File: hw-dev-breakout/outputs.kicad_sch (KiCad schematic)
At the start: 67 parts, among them J301 WAGO 250-220, J302 Conn_01x20, Q301 2N7002, Q302 2N7002, Q303 2N7002, Q304 2N7002, Q305 2N7002, Q306 2N7002, Q307 2N7002, Q308 HL 20N04, Q309 HL 20N04, Q310 2N7002, Q311 Q_PMOS_HL_4485

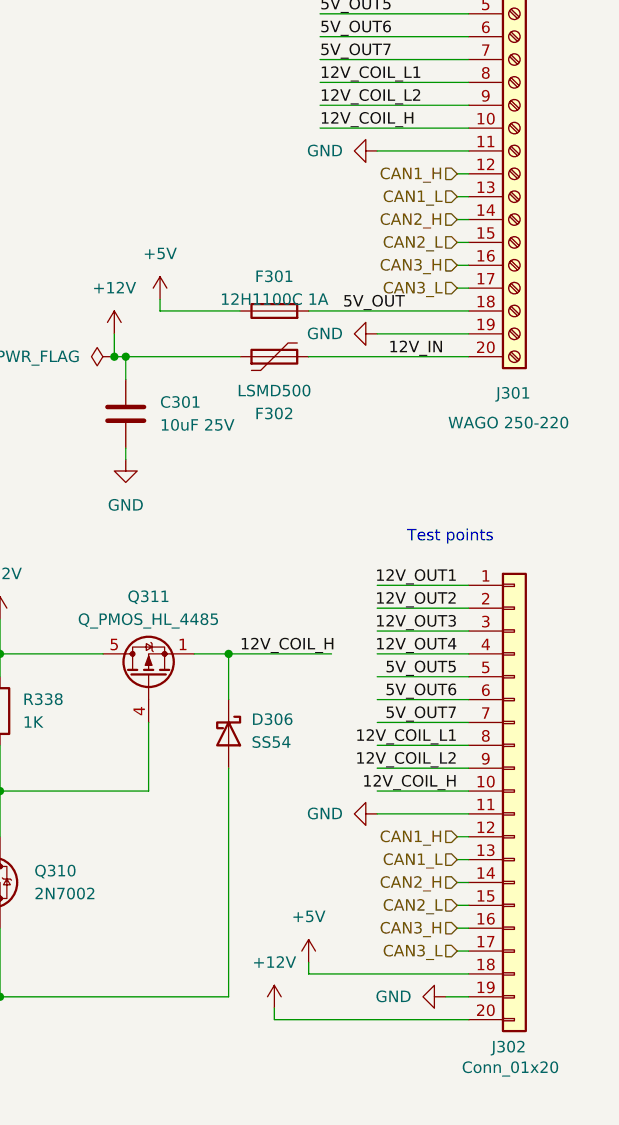
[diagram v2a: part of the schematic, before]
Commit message: pcb: Partially routed
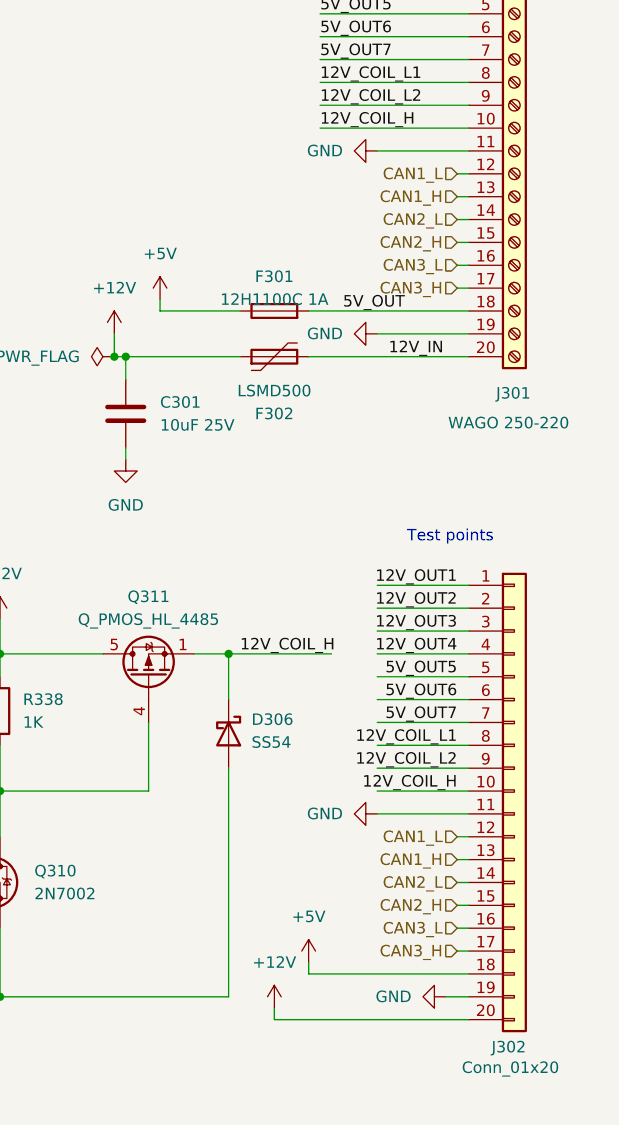
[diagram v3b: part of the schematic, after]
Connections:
- net CAN1_H: now also J301.13 (Pin_13), J302.13 (Pin_13); no longer J301.12 (Pin_12), J302.12 (Pin_12)
- net CAN1_L: now also J301.12 (Pin_12), J302.12 (Pin_12); no longer J301.13 (Pin_13), J302.13 (Pin_13)
- net CAN2_H: now also J301.15 (Pin_15), J302.15 (Pin_15); no longer J301.14 (Pin_14), J302.14 (Pin_14)
- net CAN2_L: now also J301.14 (Pin_14), J302.14 (Pin_14); no longer J301.15 (Pin_15), J302.15 (Pin_15)
- net CAN3_H: now also J301.17 (Pin_17), J302.17 (Pin_17); no longer J301.16 (Pin_16), J302.16 (Pin_16)
- net CAN3_L: now also J301.16 (Pin_16), J302.16 (Pin_16); no longer J301.17 (Pin_17), J302.17 (Pin_17)
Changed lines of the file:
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@@
 	(hierarchical_label "CAN3_H"
 		(shape input)
+		(at 269.24 143.51 180)
+		(fields_autoplaced yes)
+		(effects
+			(font
+				(size 1.27 1.27)
+			)
+			(justify right)
+		)
+	)
+	(hierarchical_label "OUT3"
+		(shape input)
+		(at 80.01 54.61 180)
+		(fields_autoplaced yes)
+		(effects
+			(font
+				(size 1.27 1.27)
+			)
+			(justify right)
+		)
+	)
+	(hierarchical_label "COIL_L2"
+		(shape input)
+		(at 148.59 62.23 180)
+		(fields_autoplaced yes)
+		(effects
+			(font
+				(size 1.27 1.27)
+			)
+			(justify right)
+		)
+	)
+	(hierarchical_label "CAN2_H"
+		(shape input)
+		(at 269.24 138.43 180)
+		(fields_autoplaced yes)
+		(effects
+			(font
+				(size 1.27 1.27)
+			)
+			(justify right)
+		)
+	)
+	(hierarchical_label "OUT1"
+		(shape input)
+		(at 21.59 53.34 180)
+		(fields_autoplaced yes)
+		(effects
+			(font
+				(size 1.27 1.27)
+			)
+			(justify right)
+		)
+	)
+	(hierarchical_label "CAN1_L"
+		(shape input)
+		(at 269.24 130.81 180)
+		(fields_autoplaced yes)
+		(effects
+			(font
+				(size 1.27 1.27)
+			)
+			(justify right)
+		)
+	)
+	(hierarchical_label "OUT7"
+		(shape input)
+		(at 130.81 165.1 180)
+		(fields_autoplaced yes)
+		(effects
+			(font
+				(size 1.27 1.27)
+			)
+			(justify right)
+		)
+	)
+	(hierarchical_label "CAN1_L"
+		(shape input)
+		(at 269.24 57.15 180)
+		(fields_autoplaced yes)
+		(effects
+			(font
+				(size 1.27 1.27)
+			)
+			(justify right)
+		)
+	)
+	(hierarchical_label "CAN2_H"
+		(shape input)
+		(at 269.24 64.77 180)
+		(fields_autoplaced yes)
+		(effects
+			(font
+				(size 1.27 1.27)
+			)
+			(justify right)
+		)
+	)
+	(hierarchical_label "CAN2_L"
+		(shape input)
+		(at 269.24 62.23 180)
+		(fields_autoplaced yes)
+		(effects
+			(font
+				(size 1.27 1.27)
+			)
+			(justify right)
+		)
+	)
+	(hierarchical_label "CAN3_H"
+		(shape input)
+		(at 269.24 69.85 180)
+		(fields_autoplaced yes)
+		(effects
+			(font
+				(size 1.27 1.27)
+			)
+			(justify right)
+		)
+	)
+	(hierarchical_label "CAN1_H"
+		(shape input)
+		(at 269.24 133.35 180)
+		(fields_autoplaced yes)
+		(effects
+			(font
+				(size 1.27 1.27)
+			)
+			(justify right)
+		)
+	)
+	(hierarchical_label "CAN3_L"
+		(shape input)
+		(at 269.24 67.31 180)
+		(fields_autoplaced yes)
+		(effects
+			(font
+				(size 1.27 1.27)
+			)
+			(justify right)
+		)
+	)
+	(hierarchical_label "COIL_H"
+		(shape input)
+		(at 187.96 135.89 180)
+		(fields_autoplaced yes)
+		(effects
+			(font
+				(size 1.27 1.27)
+			)
+			(justify right)
+		)
+	)
+	(hierarchical_label "CAN3_L"
+		(shape input)
 		(at 269.24 140.97 180)
 		(fields_autoplaced yes)
@@
 		)
 	)
-	(hierarchical_label "OUT3"
-		(shape input)
-		(at 80.01 54.61 180)
-		(fields_autoplaced yes)
-		(effects
-			(font
-				(size 1.27 1.27)
-			)
-			(justify right)
-		)
-	)
-	(hierarchical_label "COIL_L2"
-		(shape input)
-		(at 148.59 62.23 180)
-		(fields_autoplaced yes)
-		(effects
-			(font
-				(size 1.27 1.27)
-			)
-			(justify right)
-		)
-	)
-	(hierarchical_label "CAN2_H"
+	(hierarchical_label "OUT4"
+		(shape input)
+		(at 80.01 107.95 180)
+		(fields_autoplaced yes)
+		(effects
+			(font
+				(size 1.27 1.27)
+			)
+			(justify right)
+		)
+	)
+	(hierarchical_label "CAN2_L"
 		(shape input)
 		(at 269.24 135.89 180)
@@
 		)
 	)
-	(hierarchical_label "OUT1"
-		(shape input)
-		(at 21.59 53.34 180)
-		(fields_autoplaced yes)
-		(effects
-			(font
-				(size 1.27 1.27)
-			)
-			(justify right)
-		)
-	)
-	(hierarchical_label "CAN1_L"
-		(shape input)
-		(at 269.24 133.35 180)
-		(fields_autoplaced yes)
-		(effects
-			(font
-				(size 1.27 1.27)
-			)
-			(justify right)
-		)
-	)
-	(hierarchical_label "OUT7"
-		(shape input)
-		(at 130.81 165.1 180)
-		(fields_autoplaced yes)
-		(effects
-			(font
-				(size 1.27 1.27)
-			)
-			(justify right)
-		)
-	)
-	(hierarchical_label "CAN1_L"
+	(hierarchical_label "OUT2"
+		(shape input)
+		(at 21.59 106.68 180)
+		(fields_autoplaced yes)
+		(effects
+			(font
+				(size 1.27 1.27)
+			)
+			(justify right)
+		)
+	)
+	(hierarchical_label "CAN1_H"
 		(shape input)
 		(at 269.24 59.69 180)
 		(fields_autoplaced yes)
 		(effects
-			(font
-				(size 1.27 1.27)
-			)
-			(justify right)
-		)
-	)
-	(hierarchical_label "CAN2_H"
-		(shape input)
-		(at 269.24 62.23 180)
-		(fields_autoplaced yes)
-		(effects
-			(font
-				(size 1.27 1.27)
-			)
-			(justify right)
-		)
-	)
-	(hierarchical_label "CAN2_L"
-		(shape input)
-		(at 269.24 64.77 180)
-		(fields_autoplaced yes)
-		(effects
-			(font
-				(size 1.27 1.27)
-			)
-			(justify right)
-		)
-	)
-	(hierarchical_label "CAN3_H"
-		(shape input)
-		(at 269.24 67.31 180)
-		(fields_autoplaced yes)
-		(effects
-			(font
-				(size 1.27 1.27)
-			)
-			(justify right)
-		)
-	)
-	(hierarchical_label "CAN1_H"
-		(shape input)
-		(at 269.24 130.81 180)
-		(fields_autoplaced yes)
-		(effects
-			(font
-				(size 1.27 1.27)
-			)
-			(justify right)
-		)
-	)
-	(hierarchical_label "CAN3_L"
-		(shape input)
-		(at 269.24 69.85 180)
-		(fields_autoplaced yes)
-		(effects
-			(font
-				(size 1.27 1.27)
-			)
-			(justify right)
-		)
-	)
-	(hierarchical_label "COIL_H"
-		(shape input)
-		(at 187.96 135.89 180)
-		(fields_autoplaced yes)
-		(effects
-			(font
-				(size 1.27 1.27)
-			)
-			(justify right)
-		)
-	)
-	(hierarchical_label "CAN3_L"
-		(shape input)
-		(at 269.24 143.51 180)
-		(fields_autoplaced yes)
-		(effects
-			(font
-				(size 1.27 1.27)
-			)
-			(justify right)
-		)
-	)
-	(hierarchical_label "OUT4"
-		(shape input)
-		(at 80.01 107.95 180)
-		(fields_autoplaced yes)
-		(effects
-			(font
-				(size 1.27 1.27)
-			)
-			(justify right)
-		)
-	)
-	(hierarchical_label "CAN2_L"
-		(shape input)
-		(at 269.24 138.43 180)
-		(fields_autoplaced yes)
-		(effects
-			(font
-				(size 1.27 1.27)
-			)
-			(justify right)
-		)
-	)
-	(hierarchical_label "OUT2"
-		(shape input)
-		(at 21.59 106.68 180)
-		(fields_autoplaced yes)
-		(effects
-			(font
-				(size 1.27 1.27)
-			)
-			(justify right)
-		)
-	)
-	(hierarchical_label "CAN1_H"
-		(shape input)
-		(at 269.24 57.15 180)
-		(fields_autoplaced yes)
-		(effects

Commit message: pcb: Routed for 2 layer, fixed P-fet error
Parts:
- J301: footprint hw-dev-breakout:CONN-TH_250-220 -> hw-dev-breakout:WAGO 250-22
- J302: now not fitted
- Q308, Q309: footprint Package_TO_SOT_SMD:TO-252-3_TabPin2 -> Package_TO_SOT_SMD:TO-252-2
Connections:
- net +12V: now also Q311.1 (S), Q311.2 (S), Q311.3 (S); no longer Q311.5 (D), Q311.6 (D), Q311.7 (D), Q311.8 (D)
- net 12V_COIL_H: now also Q311.5 (D), Q311.6 (D), Q311.7 (D), Q311.8 (D); no longer Q311.1 (S), Q311.2 (S), Q311.3 (S)
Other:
- moved on the sheet: Q311
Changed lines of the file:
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@@
 			)
 		)
-		(property "Footprint" "Package_TO_SOT_SMD:TO-252-3_TabPin2"
+		(property "Footprint" "Package_TO_SOT_SMD:TO-252-2"
 			(at 184.15 30.48 0)
 			(effects
@@
 			)
 		)
-		(property "Footprint" "Package_TO_SOT_SMD:TO-252-3_TabPin2"
+		(property "Footprint" "Package_TO_SOT_SMD:TO-252-2"
 			(at 184.15 59.69 0)
 			(effects
@@
 		(in_bom yes)
 		(on_board yes)
-		(dnp no)
+		(dnp yes)
 		(property "Reference" "J302"
 			(at 273.05 154.178 0)
@@
 	(symbol
 		(lib_id "hw-dev-breakout:Q_PMOS_HL_4485")
-		(at 234.95 113.03 90)
+		(at 234.95 113.03 270)
+		(mirror x)
 		(unit 1)
 		(exclude_from_sim no)
@@
 		(on_board yes)
 		(dnp no)
-		(fields_autoplaced yes)
 		(property "Reference" "Q311"
 			(at 234.95 104.14 90)
@@
 		)
 		(property "Footprint" "Package_SO:SOP-8_3.9x4.9mm_P1.27mm"
-			(at 247.904 109.982 0)
+			(at 221.996 109.982 0)
 			(effects
 				(font
@@
 		)
 		(property "Datasheet" "https://www.lcsc.com/datasheet/lcsc_datasheet_2310251707_HL-4485_C7499854.pdf"
-			(at 250.19 112.014 0)
+			(at 219.71 112.014 0)
 			(effects
 				(font
@@
 		)
 		(property "Description" "High cell density trenched P-ch MOSFET"
-			(at 248.666 111.76 0)
+			(at 221.234 111.76 0)
 			(effects
 				(font
@@
 			)
 		)
-		(property "Footprint" "hw-dev-breakout:CONN-TH_250-220"
+		(property "Footprint" "hw-dev-breakout:WAGO 250-22"
 			(at 275.59 52.07 0)
 			(effects

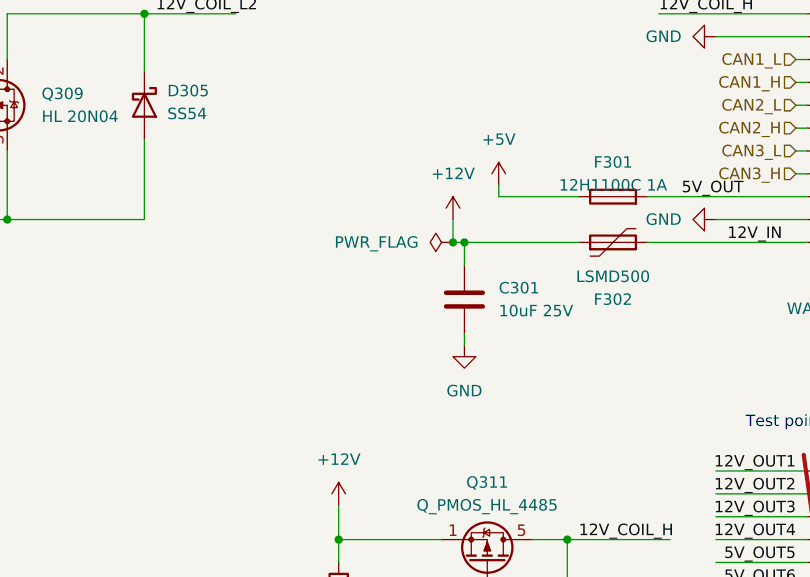
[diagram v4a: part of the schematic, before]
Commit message: Add reverse polarity protection for 12V In
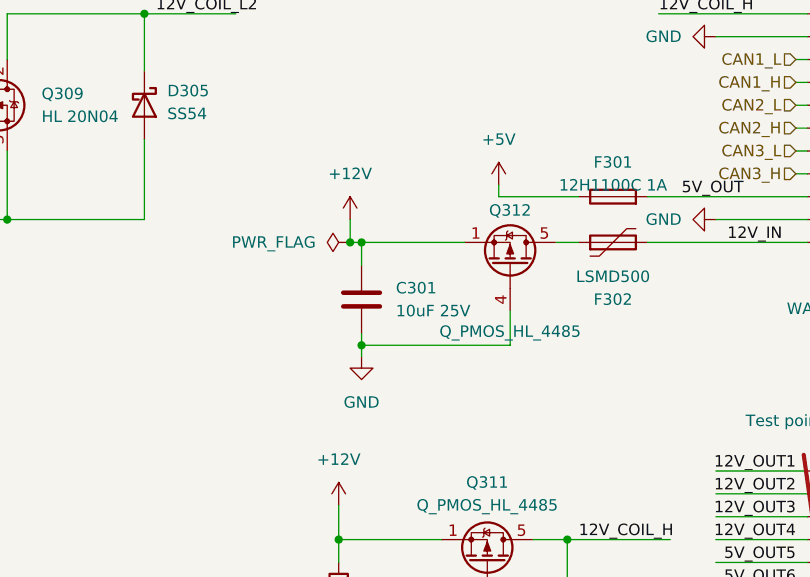
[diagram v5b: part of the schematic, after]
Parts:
- added Q312: Q_PMOS_HL_4485, Package_SO:SOP-8_3.9x4.9mm_P1.27mm, symbol hw-dev-breakout:Q_PMOS_HL_4485
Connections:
- net +12V: now also Q312.1 (S), Q312.2 (S), Q312.3 (S); no longer F302.1
- net GND: now also Q312.4 (G)
- new net: F302.1, Q312.5 (D), Q312.6 (D), Q312.7 (D), Q312.8 (D)
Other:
- moved on the sheet: C301
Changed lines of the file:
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@@
 	)
 	(junction
+		(at 220.98 88.9)
+		(diameter 0)
+		(color 0 0 0 0)
+	)
+	(junction
 		(at 196.85 22.86)
 		(diameter 0)
@@
 	)
 	(junction
+		(at 220.98 77.47)
+		(diameter 0)
+		(color 0 0 0 0)
+	)
+	(junction
 		(at 198.12 135.89)
 		(diameter 0)
@@
 	)
 	(junction
-		(at 231.14 77.47)
+		(at 219.71 77.47)
 		(diameter 0)
 		(color 0 0 0 0)
@@
 		(color 0 0 0 0)
 	)
-	(junction
-		(at 232.41 77.47)
-		(diameter 0)
-		(color 0 0 0 0)
-	)
 	(wire
 		(pts
@@
 	(wire
 		(pts
+			(xy 237.49 85.09) (xy 237.49 88.9)
+		)
+		(stroke
+			(width 0)
+			(type default)
+		)
+	)
+	(wire
+		(pts
 			(xy 48.26 24.13) (xy 48.26 25.4)
 		)
@@
 	(wire
 		(pts
+			(xy 220.98 88.9) (xy 220.98 90.17)
+		)
+		(stroke
+			(width 0)
+			(type default)
+		)
+	)
+	(wire
+		(pts
 			(xy 161.29 62.23) (xy 161.29 63.5)
 		)
@@
 	(wire
 		(pts
+			(xy 220.98 87.63) (xy 220.98 88.9)
+		)
+		(stroke
+			(width 0)
+			(type default)
+		)
+	)
+	(wire
+		(pts
 			(xy 161.29 71.12) (xy 161.29 74.93)
 		)
@@
 	(wire
 		(pts
-			(xy 232.41 77.47) (xy 245.11 77.47)
-		)
-		(stroke
-			(width 0)
-			(type default)
-		)
-	)
-	(wire
-		(pts
 			(xy 48.26 33.02) (xy 48.26 35.56)
 		)
@@
 	(wire
 		(pts
+			(xy 237.49 88.9) (xy 220.98 88.9)
+		)
+		(stroke
+			(width 0)
+			(type default)
+		)
+	)
+	(wire
+		(pts
 			(xy 161.29 33.02) (xy 161.29 34.29)
 		)
@@
 	(wire
 		(pts
-			(xy 232.41 77.47) (xy 232.41 80.01)
+			(xy 220.98 77.47) (xy 220.98 80.01)
 		)
 		(stroke
@@
 	(wire
 		(pts
-			(xy 231.14 77.47) (xy 232.41 77.47)
+			(xy 219.71 77.47) (xy 220.98 77.47)
 		)
 		(stroke
@@
 	(wire
 		(pts
-			(xy 231.14 74.93) (xy 231.14 77.47)
+			(xy 219.71 74.93) (xy 219.71 77.47)
 		)
 		(stroke
@@
 	(wire
 		(pts
-			(xy 232.41 87.63) (xy 232.41 88.9)
-		)
-		(stroke
-			(width 0)
-			(type default)
-		)
-	)
-	(wire
-		(pts
 			(xy 157.48 160.02) (xy 157.48 154.94)
 		)
@@
 	(wire
 		(pts
+			(xy 220.98 77.47) (xy 232.41 77.47)
+		)
+		(stroke
+			(width 0)
+			(type default)
+		)
+	)
+	(wire
+		(pts
+			(xy 242.57 77.47) (xy 245.11 77.47)
+		)
+		(stroke
+			(width 0)
+			(type default)
+		)
+	)
+	(wire
+		(pts
 			(xy 48.26 66.04) (xy 48.26 58.42)
 		)
@@
 	(symbol
 		(lib_id "Device:C")
-		(at 232.41 83.82 0)
+		(at 220.98 83.82 0)
 		(unit 1)
 		(exclude_from_sim no)
@@
 		(fields_autoplaced yes)
 		(property "Reference" "C301"
-			(at 236.22 82.5499 0)
+			(at 224.79 82.5499 0)
 			(effects
 				(font
@@
 		)
 		(property "Value" "10uF 25V"
-			(at 236.22 85.0899 0)
+			(at 224.79 85.0899 0)
 			(effects
 				(font
@@
 		)
 		(property "Footprint" "Capacitor_SMD:CP_Elec_4x4.5"
-			(at 233.3752 87.63 0)
+			(at 221.9452 87.63 0)
 			(effects
 				(font
@@
 		)
 		(property "Datasheet" "~"
-			(at 232.41 83.82 0)
+			(at 220.98 83.82 0)
 			(effects
 				(font
@@
 		)
 		(property "Description" "Unpolarized capacitor"
-			(at 232.41 83.82 0)
+			(at 220.98 83.82 0)
 			(effects
 				(font
@@
 	(symbol
 		(lib_id "power:GND")
-		(at 232.41 88.9 0)
+		(at 220.98 90.17 0)
 		(unit 1)
 		(exclude_from_sim no)
@@
 		(fields_autoplaced yes)
 		(property "Reference" "#PWR0320"
-			(at 232.41 95.25 0)
+			(at 220.98 96.52 0)
 			(effects
 				(font
@@
 		)
 		(property "Value" "GND"
-			(at 232.41 93.98 0)
+			(at 220.98 95.25 0)
 			(effects
 				(font
@@
 		)
 		(property "Footprint" ""
-			(at 232.41 88.9 0)
+			(at 220.98 90.17 0)
 			(effects
 				(font
@@
 		)
 		(property "Datasheet" ""
-			(at 232.41 88.9 0)
+			(at 220.98 90.17 0)
 			(effects
 				(font
@@
 		)
 		(property "Description" "Power symbol creates a global label with name \"GND\" , ground"
-			(at 232.41 88.9 0)
+			(at 220.98 90.17 0)
 			(effects
 				(font
@@
 	(symbol
 		(lib_id "power:+12V")
-		(at 231.14 74.93 0)
+		(at 219.71 74.93 0)
 		(unit 1)
 		(exclude_from_sim no)
@@
 		(fields_autoplaced yes)
 		(property "Reference" "#PWR0319"
-			(at 231.14 78.74 0)
+			(at 219.71 78.74 0)
 			(effects
 				(font
@@
 		)
 		(property "Value" "+12V"
-			(at 231.14 69.85 0)
+			(at 219.71 69.85 0)
 			(effects
 				(font
@@
 		)
 		(property "Footprint" ""
-			(at 231.14 74.93 0)
+			(at 219.71 74.93 0)
 			(effects
 				(font
@@
 		)
 		(property "Datasheet" ""
-			(at 231.14 74.93 0)
+			(at 219.71 74.93 0)
 			(effects
 				(font
@@
 		)
 		(property "Description" "Power symbol creates a global label with name \"+12V\""
-			(at 231.14 74.93 0)
+			(at 219.71 74.93 0)
 			(effects
 				(font
@@
 	)
 	(symbol
+		(lib_id "hw-dev-breakout:Q_PMOS_HL_4485")
+		(at 237.49 80.01 270)
+		(mirror x)
+		(unit 1)
+		(exclude_from_sim no)
+		(in_bom yes)
+		(on_board yes)
+		(dnp no)
+		(property "Reference" "Q312"
+			(at 237.49 73.914 90)
+			(effects
+				(font
+					(size 1.27 1.27)
+				)
+			)
+		)
+		(property "Value" "Q_PMOS_HL_4485"
+			(at 237.49 87.376 90)
+			(effects
+				(font
+					(size 1.27 1.27)
+				)
+			)
+		)
+		(property "Footprint" "Package_SO:SOP-8_3.9x4.9mm_P1.27mm"
+			(at 224.536 76.962 0)
+			(effects
+				(font
+					(size 1.27 1.27)
+				)
+				(hide yes)
+			)
+		)
+		(property "Datasheet" "https://www.lcsc.com/datasheet/lcsc_datasheet_2310251707_HL-4485_C7499854.pdf"
+			(at 222.25 78.994 0)
+			(effects
+				(font
+					(size 1.27 1.27)
+				)
+				(hide yes)
+			)
+		)
+		(property "Description" "High cell density trenched P-ch MOSFET"
+			(at 223.774 78.74 0)
+			(effects
+				(font
+					(size 1.27 1.27)
+				)
+				(hide yes)
+			)
+		)
+		(pin "7"
+		)
+		(pin "1"
+		)
+		(pin "8"
+		)
+		(pin "4"
+		)
+		(pin "2"
+		)
+		(pin "3"
+		)
+		(pin "6"
+		)
+		(pin "5"
+		)
+		(instances
+			(project "hw-dev-breakout"
+				(path "/da5a1e6a-2605-436b-a30c-1027586d5c0a/1f1f44b3-ef48-4473-b342-ce0161e9e20c"
+					(reference "Q312")
+					(unit 1)
+				)
+			)
+		)
+	)
+	(symbol
 		(lib_id "Jumper:SolderJumper_2_Open")
 		(at 157.48 151.13 90)
@@
 	(symbol
 		(lib_id "power:PWR_FLAG")
-		(at 231.14 77.47 90)
+		(at 219.71 77.47 90)
 		(unit 1)
 		(exclude_from_sim no)
@@
 		(fields_autoplaced yes)
 		(property "Reference" "#FLG0301"
-			(at 229.235 77.47 0)
+			(at 217.805 77.47 0)
 			(effects
 				(font
@@
 		)
 		(property "Value" "PWR_FLAG"
-			(at 227.33 77.4699 90)
+			(at 215.9 77.4699 90)
 			(effects
 				(font
@@
 		)
 		(property "Footprint" ""
-			(at 231.14 77.47 0)
+			(at 219.71 77.47 0)
 			(effects
 				(font
@@
 		)
 		(property "Datasheet" "~"
-			(at 231.14 77.47 0)
+			(at 219.71 77.47 0)
 			(effects
 				(font
@@
 		)
 		(property "Description" "Special symbol for telling ERC where power comes from"
-			(at 231.14 77.47 0)
+			(at 219.71 77.47 0)
 			(effects
 				(font

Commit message: Final cleanups for initial fab run
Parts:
- C301: 'JLCPCB Rotation Offset (none) -> -180; LCSC Part # (none) -> C4747969
- D301, D302, D303: value ORANGE -> LED_YELLOW; LCSC Part # (none) -> C72038
- D304, D305, D306: LCSC Part # (none) -> C22452
- F301: value 12H1100C 1A -> 12H1100C (1A); LCSC Part # (none) -> C182308
- F302: LCSC Part # (none) -> C262045
- J301: LCSC Part # (none) -> C2833599
- JP301, JP302, JP303, JP304, JP305, JP306, JP307: now not fitted
- Q301, Q302, Q303, Q304, Q305, Q306, Q307, Q310: LCSC Part # (none) -> C8545
- Q308, Q309: value HL 20N04 -> HD60N03; Alternate (none) -> NTD5867NL; LCSC Part # (none) -> C216259
- Q311, Q312: LCSC Part # (none) -> C7499854
- R301, R302, R303, R313, R314, R315, R325, R330, R331, R336: LCSC Part # (none) -> C25804
- R304, R305, R306, R316, R317, R318, R326, R332, R333, R337: LCSC Part # (none) -> C23140
- R307, R308, R309, R319, R320, R321, R329, R338: LCSC Part # (none) -> C21190
- R310, R311, R312, R322, R323, R324, R334: LCSC Part # (none) -> C175280
- R327, R328, R335: LCSC Part # (none) -> C23138
